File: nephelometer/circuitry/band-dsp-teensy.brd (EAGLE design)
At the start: 74 x 55 mm, 47 parts, among them IC1 LM4041CILP, IC2 AD822N, IC3 MCP6S21, J1 RJ11-6PTH, Q1 IRLB8721, T1 2N2222, T2 2N2222

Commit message: Separate 3V3 supply for analog circuits. Guard ring for TIA
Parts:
- added C10: 1µF, adafruit:C025-030X050
- added IC4: LP2950ACZ-3.3, v-reg:TO92
- C3: device adafruit:C050-024X044 -> adafruit:C025-025X050
- C8: device adafruit:C025-030X050 -> adafruit:E2,5-5
- moved R14 16.5 mm to (66.2, 20.6)
- moved C1 3.54 mm to (24.5, 30.5)
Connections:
- new net N$2: BRD1.3.3V, R14.1
- net +3V3: now also C8.+, IC4.1; no longer BRD1.3.3V, C8.1, R14.1
- net +5V: now also C10.1, IC4.3
- net GND: now also C10.2, C8.-, IC4.2; no longer C8.2
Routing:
- net 1V65: track 128.3 -> 177.4 mm
- net +5V: track 108.2 -> 143.0 mm
- net +3V3: track 158.2 -> 130.8 mm
- net N$2: track 0.00 -> 8.68 mm
- net GND: track 283.8 -> 289.0 mm
- net N$11: track 12.8 -> 14.2 mm

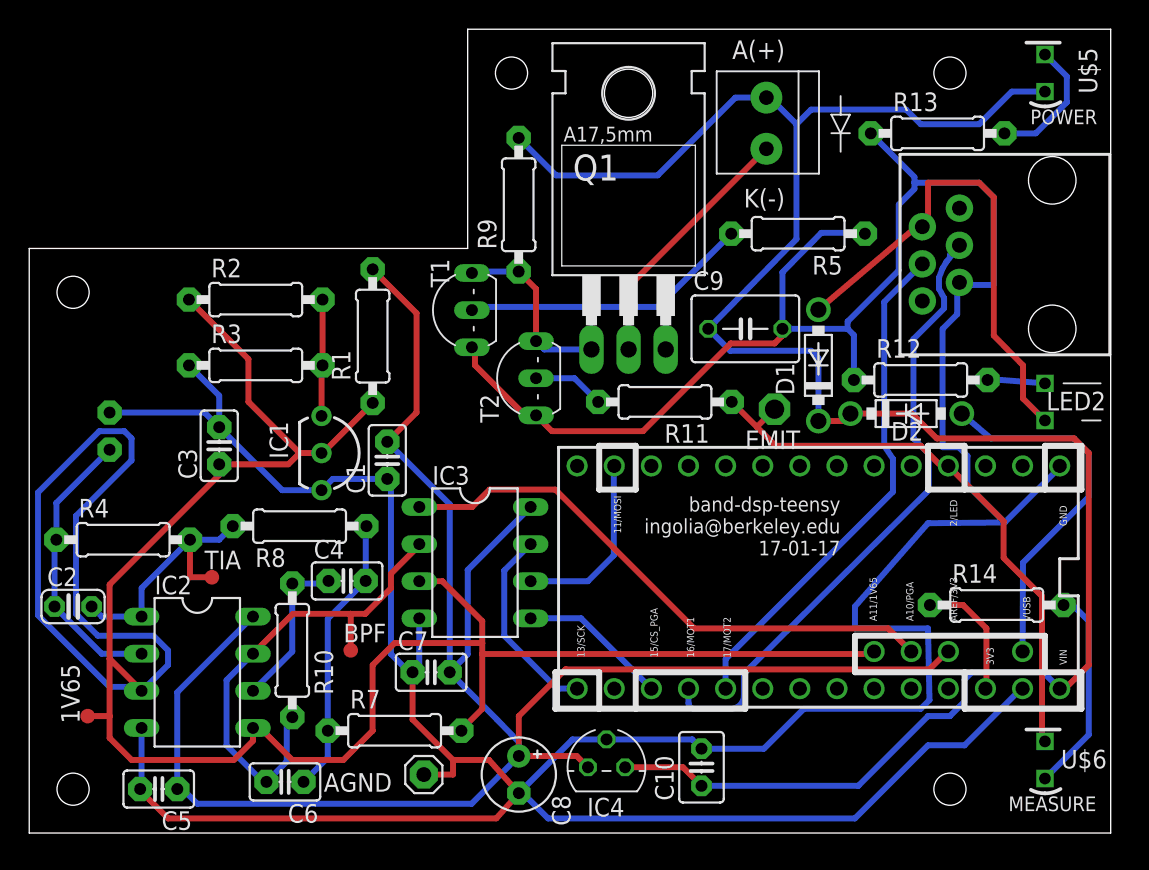
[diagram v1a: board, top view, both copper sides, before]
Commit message: Feather-based board with external ADC
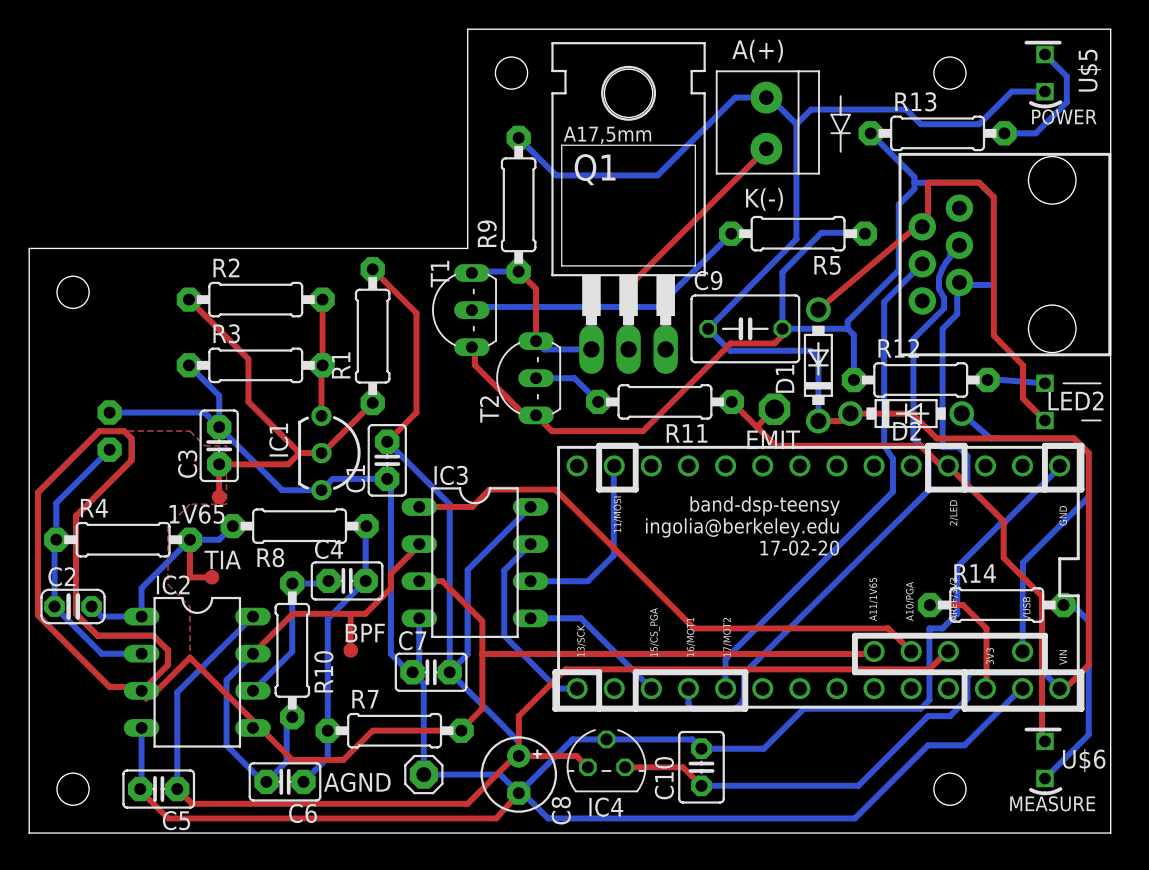
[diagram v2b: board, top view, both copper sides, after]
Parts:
- moved 1V65 17.5 mm to (13.0, 28.0), turned to 180 degrees
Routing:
- net 1V65: track 177.4 -> 195.8 mm
- net GND: track 289.0 -> 278.4 mm
- added copper zone on layer 1, net 1V65
- added copper zone on layer 16, net 1V65
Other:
- board text added: "band-dsp-teensy ingolia@berkeley.edu 17-02-20"
- board text removed: "band-dsp-teensy ingolia@berkeley.edu 17-01-17"
